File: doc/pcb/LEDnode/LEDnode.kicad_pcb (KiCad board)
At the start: 2 copper layers, 44 x 42.5 mm, 33 parts, among them J1 LI BAT, Q1 BC807, Q2 BC807, Q3 BC807, Q4 BC807, SW1 RotaryEncoder_Switch, U1 STM32G071KxT, U2 AF-02841BMR-B, U3 LM393, U4 AP1603, U5 BME280, U6 LIS3MDL, Y1 32k768

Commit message: ...
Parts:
- removed U3: LM393, Package_SO:SOP-8_3.9x4.9mm_P1.27mm
- added C15: 104, Capacitor_SMD:C_0603_1608Metric, F.Cu at (79.7, 104.4)
- added C16: 104, Capacitor_SMD:C_0603_1608Metric, F.Cu at (71.7, 106.9)
- added C17: 104, Capacitor_SMD:C_0603_1608Metric, F.Cu at (79.7, 101.9)
- added C18: 104, Capacitor_SMD:C_0603_1608Metric, F.Cu at (75.7, 101.9)
- added C19: 104, Capacitor_SMD:C_0603_1608Metric, F.Cu at (79.7, 107.0)
- added C20: 104, Capacitor_SMD:C_0603_1608Metric, F.Cu at (55.6, 114.6)
- added D1: MBR0530, Diode_SMD:D_SOD-123, F.Cu at (75.0, 99.0)
- added D2: LED2, LED_SMD:LED_0603_1608Metric, F.Cu at (60.5, 107.0)
- added D3: LED1, LED_SMD:LED_0603_1608Metric, F.Cu at (60.5, 109.6)
- added J2: SWD, Connector_PinHeader_1.27mm:PinHeader_1x05_P1.27mm_Vertical, F.Cu at (80.0, 70.0)
- added J3: GPIO1, Connector_PinHeader_2.54mm:PinHeader_1x06_P2.54mm_Vertical, F.Cu at (82.5, 74.0)
- added J4: GPIO2, Connector_PinHeader_2.54mm:PinHeader_1x08_P2.54mm_Vertical, F.Cu at (82.5, 77.5)
- added Q5: IRLML6346, Package_TO_SOT_SMD:SOT-23, F.Cu at (56.0, 106.7)
- added Q6: BSS138, Package_TO_SOT_SMD:SOT-23, F.Cu at (56.0, 111.1)
- added R10: 220, Resistor_SMD:R_0603_1608Metric, F.Cu at (72.6, 109.5)
- added R11: 220, Resistor_SMD:R_0603_1608Metric, F.Cu at (83.7, 98.6)
- added R12: MCU_INT, Resistor_SMD:R_0603_1608Metric, F.Cu at (64.5, 109.5)
- added R13: 0, Resistor_SMD:R_0603_1608Metric, F.Cu at (59.6, 114.6)
- added R14: 220R, Resistor_SMD:R_0603_1608Metric, F.Cu at (63.6, 112.1)
- added R15: MCU_INT, Resistor_SMD:R_0603_1608Metric, F.Cu at (83.7, 101.1)
- added R16: 1k, Resistor_SMD:R_0603_1608Metric, F.Cu at (68.6, 109.4)
- added R17: 1k, Resistor_SMD:R_0603_1608Metric, F.Cu at (87.7, 98.6)
- added R6: 220R, Resistor_SMD:R_0603_1608Metric, F.Cu at (51.5, 105.7)
- added R7: 10k, Resistor_SMD:R_0603_1608Metric, F.Cu at (75.7, 107.0)
- added R8: 1k, Resistor_SMD:R_0603_1608Metric, F.Cu at (76.6, 109.5)
- added R9: MCU_INT, Resistor_SMD:R_0603_1608Metric, F.Cu at (68.6, 112.0)
- added SW2: MFP 120, BartLib_Switch:MFP 120, F.Cu at (147.0, 48.5)
- added SW3: TL3342F160QG, Button_Switch_SMD:SW_SPST_B3SL-1002P, F.Cu at (146.0, 78.5)
- J1: value LI BAT -> Ni-MH
- R1: value 170k -> 10k
- R2: value 100k -> 220R
- R4: value R -> 10k
- SW1: value RotaryEncoder_Switch -> EC11J12-15P30C-SW
- U2: footprint BartLib_Display:LED 7.2mm -> BartLib_Display:LED 7.2mm SMD
- moved R1 84.3 mm to (75.7, 104.4)
- moved SW1 76.0 mm to (120.0, 67.0), turned to 180 degrees
- moved R2 67.5 mm to (67.6, 106.9)
- moved U2 50.8 mm to (95.0, 63.0)
- moved J1 36.7 mm to (81.3, 51.8)
- moved C2 27.8 mm to (154.8, 100.7)
- moved C4 27.8 mm to (137.7, 113.0)
- moved C5 27.8 mm to (145.1, 100.7)
- moved C8 27.8 mm to (127.7, 126.8)
- moved C9 27.8 mm to (131.7, 125.6)
- moved Q1 27.8 mm to (133.2, 109.6)
- moved Q2 27.8 mm to (138.1, 109.6)
- moved Q3 27.8 mm to (133.2, 114.0)
- moved R3 27.8 mm to (135.6, 118.1)
- moved R4 27.8 mm to (141.7, 113.0)
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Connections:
- net Net-(U1-Pad6) renamed /SYS_RST
- J1 pad 1: GND -> /INPUT
- J1 pad 2: /INPUT -> Net-(D1-Pad1)
- Q1 pad 1: /DIG1 -> /DISP_1
- Q1 pad 3: /DIG1 -> Net-(Q1-Pad3)
- Q2 pad 1: /DIG2 -> /DISP_2
- Q2 pad 3: /DIG2 -> Net-(Q2-Pad3)
- Q3 pad 1: /DIG3 -> /DISP_3
- Q3 pad 3: /DIG3 -> Net-(Q3-Pad3)
- Q4 pad 1: /DIG4 -> /DISP_4
- Q4 pad 3: /DIG4 -> Net-(Q4-Pad3)
- R1 pad 2: Net-(R1-Pad2) -> /ENC2
- R2 pad 1: Net-(R1-Pad2) -> Net-(R2-Pad1)
- R2 pad 2: GND -> /MODE
- SW1 pad A: unconnected-(SW1-PadA) -> Net-(SW1-PadA)
- SW1 pad B: unconnected-(SW1-PadB) -> Net-(SW1-PadB)
- SW1 pad C: unconnected-(SW1-PadC) -> Net-(SW1-PadC)
- SW1 pad S1: unconnected-(SW1-PadS1) -> Net-(SW1-PadS1)
- SW1 pad S2: unconnected-(SW1-PadS2) -> GND
- U1 pad 10: unconnected-(U1-Pad10) -> /Rx
- U1 pad 11: unconnected-(U1-Pad11) -> /ADC
- U1 pad 12: /DIG1 -> /LED2
- U1 pad 13: /DIG2 -> /DISP_B
- U1 pad 14: /DIG3 -> /DISP_3
- U1 pad 15: Net-(U1-Pad15) -> /DISP_G
- U1 pad 16: Net-(U1-Pad16) -> /DISP_C
- U1 pad 17: Net-(U1-Pad17) -> /DISP_E
- U1 pad 18: /DIG4 -> /DISP_D
- U1 pad 19: Net-(U1-Pad19) -> /DISP_DP
- U1 pad 20: unconnected-(U1-Pad20) -> /DISP_0
- U1 pad 21: /BUTTON1 -> /DISP_A
- U1 pad 22: /BUTTON2 -> /DISP_F
- U1 pad 23: unconnected-(U1-Pad23) -> /DISP_1
- U1 pad 24: unconnected-(U1-Pad24) -> /SYS_SWDIO
- U1 pad 25: unconnected-(U1-Pad25) -> /SYS_SWDCLK
- U1 pad 26: unconnected-(U1-Pad26) -> /DISP_2
- U1 pad 27: Net-(U1-Pad27) -> /MODE
- U1 pad 28: Net-(U1-Pad28) -> /BUTTON2
- U1 pad 29: Net-(U1-Pad29) -> /BUTTON1
- U1 pad 30: Net-(U1-Pad30) -> /ENC2
- U1 pad 31: Net-(U1-Pad31) -> /ENC1
- U1 pad 8: unconnected-(U1-Pad8) -> /ENCODER_ACTIVE
- U1 pad 9: unconnected-(U1-Pad9) -> /Tx
- U2 pad 1: Net-(U1-Pad28) -> /DISP_E
- U2 pad 10: Net-(U1-Pad29) -> /DISP_F
- U2 pad 11: Net-(U1-Pad15) -> /DISP_A
- U2 pad 12: /DIG1 -> Net-(Q1-Pad3)
- U2 pad 2: Net-(U1-Pad27) -> /DISP_D
- U2 pad 3: Net-(U1-Pad31) -> /DISP_DP
- U2 pad 4: Net-(U1-Pad17) -> /DISP_C
- U2 pad 5: Net-(U1-Pad30) -> /DISP_G
- U2 pad 6: /DIG4 -> Net-(Q4-Pad3)
- U2 pad 7: Net-(U1-Pad16) -> /DISP_B
- U2 pad 8: /DIG3 -> Net-(Q3-Pad3)
- U2 pad 9: /DIG2 -> Net-(Q2-Pad3)
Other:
- board size 44 x 42.5 mm -> 53.5 x 35.5 mm

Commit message: working chronograph, designed PCB
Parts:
- added H1: MountingHole_Pad, BartLib_Pad:WirePad 4mm^2 Rect, F.Cu at (129.8, 71.2)
- added H2: MountingHole_Pad, BartLib_Pad:WirePad 4mm^2 Rect, F.Cu at (78.2, 101.3)
- added H3: MountingHole_Pad, BartLib_Pad:WirePad 4mm^2 Rect, F.Cu at (129.8, 101.3)
- added H4: MountingHole_Pad, BartLib_Pad:WirePad 4mm^2 Rect, F.Cu at (78.2, 71.2)
- C1, C10, C11, C12, C15, C16, C17, C18, C19, C20, C3, C4, C6, C7, C8, C9, D1, L1, Q1, Q2, Q3, Q4, Q5, Q6, R1, R10, R11, R12, R13, R14, R15, R16, R17, R2, R3, R4, R5, R6, R7, R8, R9, U1, U4, U6: moved to B.Cu
- C105: renamed from C14; moved to B.Cu
- C13: value C -> 104; moved to B.Cu
- C2, C5: value 107 -> 476; footprint Capacitor_THT:CP_Radial_D8.0mm_P3.50mm -> Capacitor_SMD:CP_Elec_5x4.5
- Y1: footprint Crystal:Crystal_C26-LF_D2.1mm_L6.5mm_Horizontal_1EP_style1 -> Crystal:Crystal_C26-LF_D2.1mm_L6.5mm_Horizontal
- moved Q5 75.3 mm to (122.4, 71.0), turned to 180 degrees
- moved C20 73.6 mm to (126.2, 93.6), turned to 180 degrees
- moved Q6 69.6 mm to (117.5, 78.4)
- moved R13 65.9 mm to (114.6, 78.2), turned to 90 degrees
- moved SW2 65.4 mm to (101.3, 95.4), turned to 180 degrees
- moved R14 63.9 mm to (125.4, 95.9), turned to 90 degrees
- moved R6 63.5 mm to (113.3, 91.1), turned to 180 degrees
- moved R10 59.6 mm to (125.5, 82.1), turned to 90 degrees
- moved R4 55.2 mm to (91.1, 91.0)
- moved R7 54.1 mm to (124.8, 84.4)
- moved R12 52.7 mm to (113.3, 89.5), turned to 180 degrees
- moved C16 52.5 mm to (118.2, 82.8)
- moved Q1 52.3 mm to (90.6, 79.3)
- moved D1 51.9 mm to (122.1, 77.3), turned to 180 degrees
- moved C17 51.8 mm to (127.8, 82.8)
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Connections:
- J4 pad 2: /DISP_B -> /DISP_0
- J4 pad 3: /DISP_3 -> /DISP_A
- J4 pad 4: /DISP_D -> /DISP_B
- J4 pad 5: /DISP_G -> /DISP_F
- Q1 pad 1: /DISP_1 -> /DISP_0
- Q2 pad 1: /DISP_2 -> /DISP_1
- Q3 pad 1: /DISP_3 -> /DISP_2
- Q4 pad 1: /DISP_4 -> /DISP_3
- U1 pad 13: /DISP_B -> /DISP_0
- U1 pad 14: /DISP_3 -> /DISP_A
- U1 pad 15: /DISP_G -> /DISP_F
- U1 pad 16: /DISP_C -> /DISP_1
- U1 pad 17: /DISP_E -> /DISP_2
- U1 pad 18: /DISP_D -> /DISP_B
- U1 pad 19: /DISP_DP -> /DISP_3
- U1 pad 20: /DISP_0 -> /DISP_E
- U1 pad 21: /DISP_A -> /DISP_D
- U1 pad 22: /DISP_F -> /DISP_DP
- U1 pad 23: /DISP_1 -> /DISP_C
- U1 pad 26: /DISP_2 -> /DISP_G
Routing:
- net +3V3: track 0.00 -> 159.5 mm, vias 0 -> 14
- net GND: track 0.00 -> 131.7 mm, vias 0 -> 41
- net /INPUT: track 0.00 -> 103.1 mm, vias 0 -> 1
- net /SDA: track 0.00 -> 80.1 mm, vias 0 -> 4
- net /SCL: track 0.00 -> 69.0 mm, vias 0 -> 5
- net /ADC: track 0.00 -> 52.8 mm, vias 0 -> 2
- net /DISP_C: track 0.00 -> 48.7 mm, vias 0 -> 7
- net /SYS_SWDCLK: track 0.00 -> 48.0 mm, vias 0 -> 6
- net /DISP_B: track 0.00 -> 44.6 mm, vias 0 -> 2
- net /ENCODER_ACTIVE: track 0.00 -> 43.7 mm
- net /MODE: track 0.00 -> 43.2 mm, vias 0 -> 2
- net /ENC2: track 0.00 -> 38.4 mm, vias 0 -> 4
- net /ENC1: track 0.00 -> 37.5 mm, vias 0 -> 2
- net /BUTTON2: track 0.00 -> 32.1 mm, vias 0 -> 2
- net /BUTTON1: track 0.00 -> 31.2 mm, vias 0 -> 2
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- added copper zone on B.Cu, net GND
- added copper zone on F.Cu, net GND
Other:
- board size 53.5 x 35.5 mm -> 55 x 36.5 mm
- board text added: "Designed by Bart"
- board text added: "LEDnode Mk1"

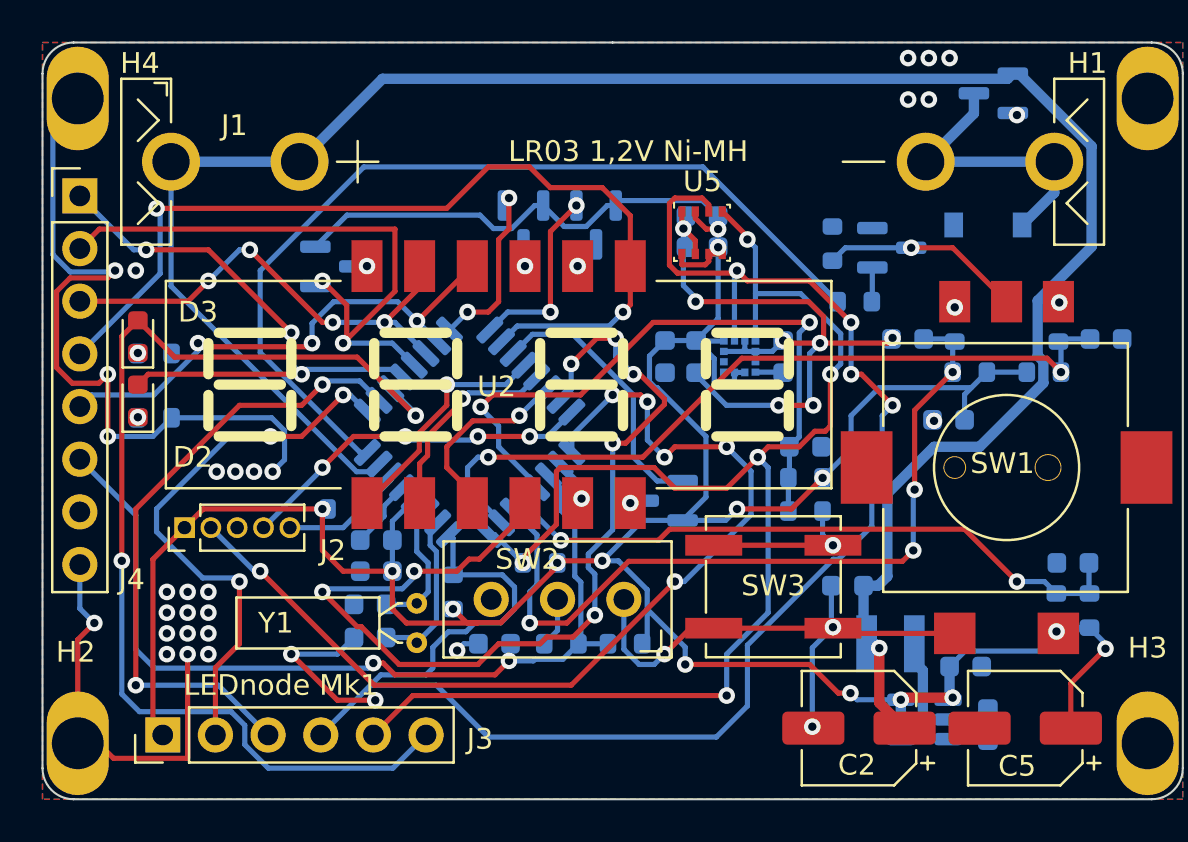
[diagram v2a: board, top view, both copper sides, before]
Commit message: added segment resistors
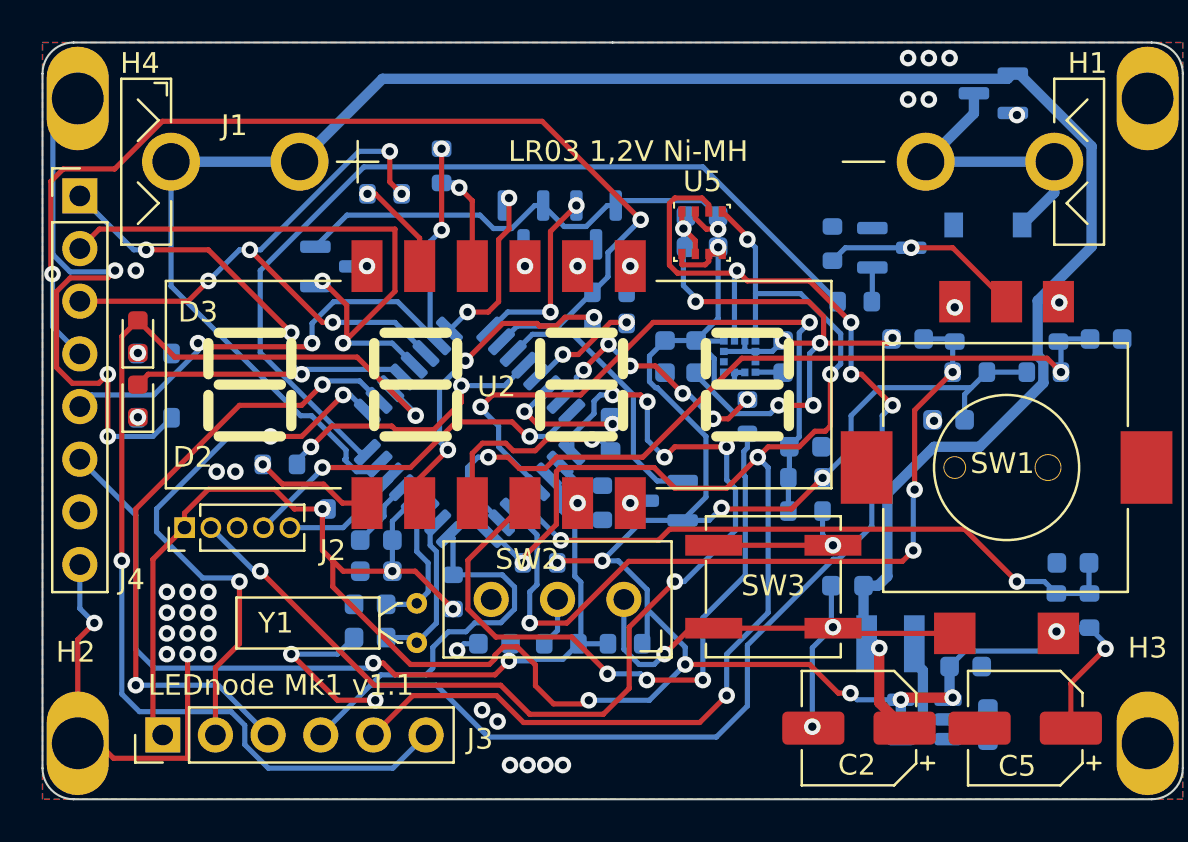
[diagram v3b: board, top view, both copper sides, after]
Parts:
- added R18: 470R, Resistor_SMD:R_0603_1608Metric, B.Cu at (93.0, 75.8)
- added R19: 470R, Resistor_SMD:R_0603_1608Metric, B.Cu at (103.8, 80.5)
- added R20: 470R, Resistor_SMD:R_0603_1608Metric, B.Cu at (110.5, 86.5)
- added R21: 470R, Resistor_SMD:R_0603_1608Metric, B.Cu at (103.8, 82.0)
- added R22: 470R, Resistor_SMD:R_0603_1608Metric, B.Cu at (88.0, 88.8)
- added R23: 470R, Resistor_SMD:R_0603_1608Metric, B.Cu at (95.8, 74.5)
- added R24: 470R, Resistor_SMD:R_0603_1608Metric, B.Cu at (103.5, 90.7)
- added R25: 470R, Resistor_SMD:R_0603_1608Metric, B.Cu at (103.9, 87.3)
- C14: renamed from C105; value C -> 105
- Q1, Q2, Q3, Q4: value BC807 -> PDTB113ET.215
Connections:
- U2 pad 1: /DISP_E -> Net-(U2-Pad1)
- U2 pad 10: /DISP_F -> Net-(U2-Pad10)
- U2 pad 11: /DISP_A -> Net-(U2-Pad11)
- U2 pad 2: /DISP_D -> Net-(U2-Pad2)
- U2 pad 3: /DISP_DP -> Net-(U2-Pad3)
- U2 pad 4: /DISP_C -> Net-(U2-Pad4)
- U2 pad 5: /DISP_G -> Net-(U2-Pad5)
- U2 pad 7: /DISP_B -> Net-(U2-Pad7)
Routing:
- net /DISP_C: track 48.7 -> 12.3 mm, vias 7 -> 6
- net Net-(U2-Pad4): track 0.00 -> 31.9 mm, vias 0 -> 3
- net Net-(U2-Pad2): track 0.00 -> 15.3 mm, vias 0 -> 3
- net +3V3: track 159.5 -> 174.4 mm, vias 14 -> 15
- net Net-(U2-Pad3): track 0.00 -> 9.87 mm, vias 0 -> 1
- net GND: track 131.7 -> 124.1 mm, vias 41 -> 45
- net /DISP_A: track 23.2 -> 30.8 mm, vias 4 -> 5
- net Net-(U2-Pad1): track 0.00 -> 5.80 mm, vias 0 -> 1
- net /DISP_B: track 44.6 -> 50.4 mm
- net /DISP_F: track 24.8 -> 30.3 mm, vias 3 -> 4
- net Net-(U2-Pad10): track 0.00 -> 4.99 mm, vias 0 -> 1
- net Net-(U2-Pad11): track 0.00 -> 4.75 mm, vias 0 -> 1
- net /DISP_D: track 9.90 -> 5.43 mm, vias 1 -> 2
- net /DISP_DP: track 9.29 -> 6.56 mm, vias 1 -> 2
- net /SYS_SWDCLK: track 48.0 -> 50.6 mm
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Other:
- board text added: "LEDnode Mk1 v1.1"
- board text removed: "LEDnode Mk1"

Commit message: new pcb
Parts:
- added C21: 476, Capacitor_SMD:CP_Elec_5x4.5, F.Cu at (108.1, 101.5)
- added C22: 476, Capacitor_SMD:CP_Elec_5x4.5, F.Cu at (100.2, 101.5)
- added H5: Copy Number, BartLib_Logo:number, B.Cu at (111.7, 72.7)
- added Q7: IRLML6346, Package_TO_SOT_SMD:SOT-23, B.Cu at (86.0, 77.1)
- added R26: 100k, Resistor_SMD:R_0603_1608Metric, B.Cu at (85.2, 81.6)
- added R27: 0, Resistor_SMD:R_0603_1608Metric, B.Cu at (83.2, 78.6)
- SW3: value TL3342F160QG -> 6x6 13; footprint Button_Switch_SMD:SW_SPST_B3SL-1002P -> Button_Switch_THT:SW_PUSH_6mm_H13mm
- moved SW3 3.93 mm to (114.9, 97.1)
- moved L1 3.18 mm to (120.2, 95.9)
- moved J3 0.60 mm to (81.8, 101.7)
- moved Q4 0.33 mm to (106.3, 90.3)
- moved R25 0.25 mm to (104.0, 87.1)
- moved SW2 0.25 mm to (101.1, 95.3)
- moved Y1 0.15 mm to (94.4, 95.5)
- moved C2 0.12 mm to (116.0, 101.6)
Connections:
- Q5 pad 1: /INPUT -> +3V3
- U1 pad 7: /INPUT -> /BACKUP
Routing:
- net /BACKUP: track 0.00 -> 22.9 mm, vias 0 -> 2
- net +3V3: track 174.4 -> 195.9 mm
- net /SDA: track 80.1 -> 92.3 mm, vias 4 -> 8
- net /SCL: track 70.1 -> 60.3 mm, vias 5 -> 6
- net GND: track 124.1 -> 133.1 mm, vias 45 -> 64
- net /SYS_SWDCLK: track 50.6 -> 59.3 mm
- net /INPUT: track 103.5 -> 106.4 mm, vias 1 -> 3
- net Net-(L1-Pad2): track 5.56 -> 8.05 mm
- net /ADC: track 52.8 -> 50.8 mm, vias 2 -> 3
- net Net-(R20-Pad2): track 31.9 -> 30.6 mm, vias 3 -> 1
- net /MODE: track 43.2 -> 44.4 mm, vias 2 -> 4
- net Net-(R6-Pad1): track 7.61 -> 8.32 mm, vias 1 -> 0
- net /ENCODER_ACTIVE: track 43.7 -> 43.1 mm
- net /BUTTON1: track 31.2 -> 31.8 mm
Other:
- board text added: "LEDnode Mk1 v2.0"
- board text removed: "LEDnode Mk1 v1.1"
